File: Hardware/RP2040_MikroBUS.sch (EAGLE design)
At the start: 78 parts, among them J1 SWD, J3 Qwiic, J5 USB C, J6 microSD, J9 MIKROBUS_SMD_BLACK1, Q1 20V/4.2A/52mΩ/1.4W, U2 MAX17048, U3 MCP73831, U4 W25QXX128MBIT, U5 RP2040, U7 3.3V, Y2 12MHz

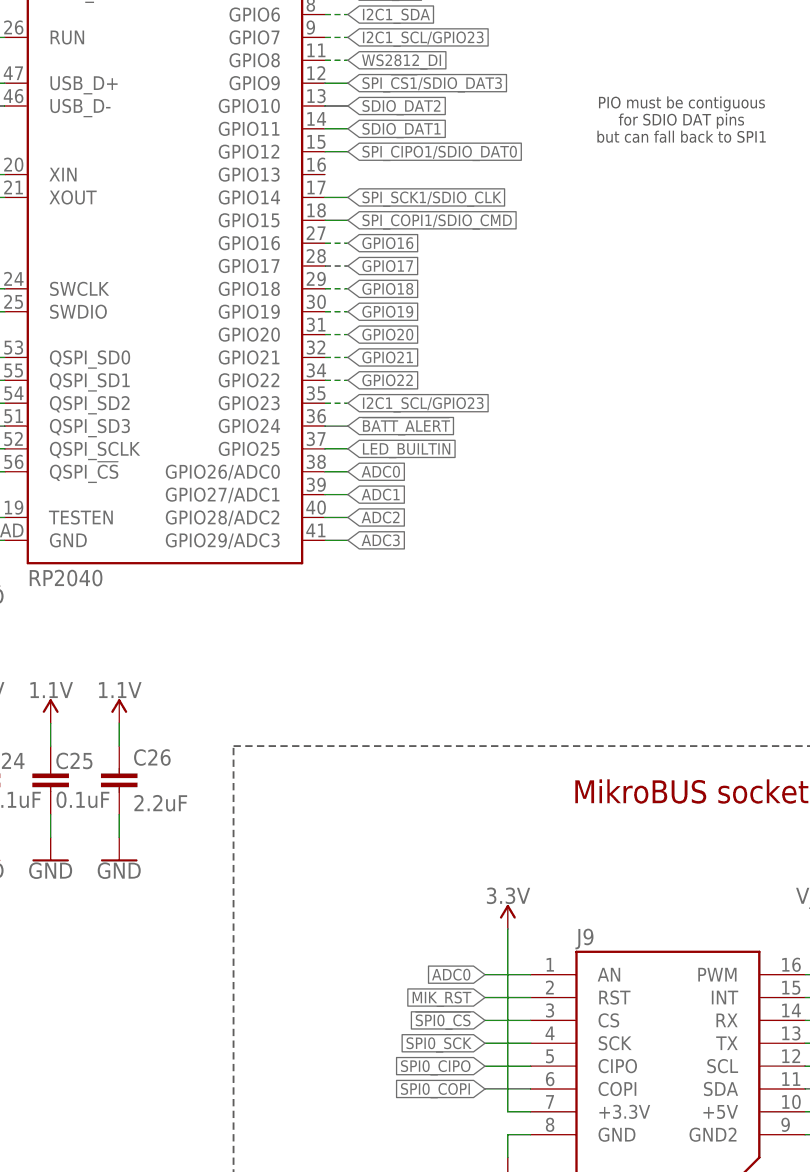
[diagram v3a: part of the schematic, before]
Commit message: From mikroE convo
* Remove reset button
* Remove CS pullup
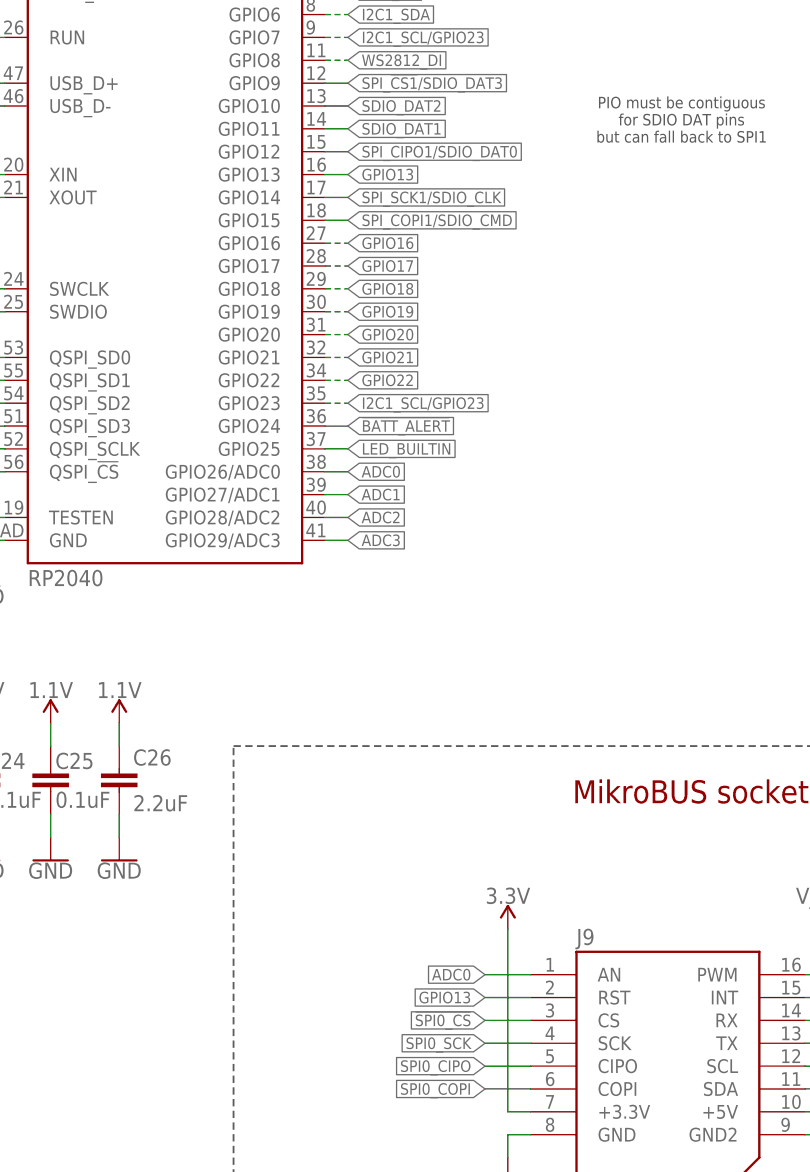
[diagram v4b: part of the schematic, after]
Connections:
- removed net MIK_RST: J9.RST
- new net GPIO13: J9.RST, U5.GPIO13
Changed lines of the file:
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@@
-</segment>
-</net>
-<net name="MIK_RST" class="0">
-<segment>
-<pinref part="J9" gate="J1" pin="RST"/>
-<wire x1="137.16" y1="38.1" x2="132.08" y2="38.1" width="0.1524" layer="91"/>
-<label x="132.08" y="38.1" size="1.27" layer="95" rot="R180" xref="yes"/>
 </segment>
 </net>
@@
 </segment>
 </net>
+<net name="GPIO13" class="0">
+<segment>
+<pinref part="U5" gate="U1" pin="GPIO13"/>
+<wire x1="114.3" y1="129.54" x2="116.84" y2="129.54" width="0.1524" layer="91"/>
+<label x="116.84" y="129.54" size="1.27" layer="95" xref="yes"/>
+</segment>
+<segment>
+<pinref part="J9" gate="J1" pin="RST"/>
+<wire x1="137.16" y1="38.1" x2="132.08" y2="38.1" width="0.1524" layer="91"/>
+<label x="132.08" y="38.1" size="1.27" layer="95" rot="R180" xref="yes"/>
+</segment>
+</net>

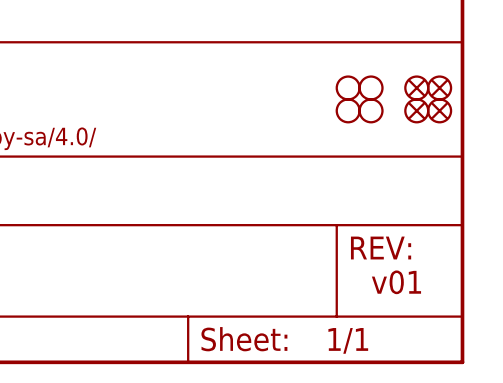
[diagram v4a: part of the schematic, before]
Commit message: Design review updates
* Bump version number
* Remove CS_PU label from borrom
* Move SWDCK TP
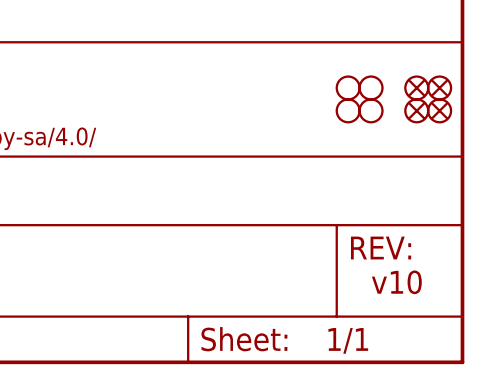
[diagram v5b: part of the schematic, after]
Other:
- note added: "v10"
- note removed: "v01"
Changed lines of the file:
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@@
 <text x="213.36" y="60.96" size="2.54" layer="94" font="vector" align="center">Status LED</text>
 <text x="381" y="101.6" size="2.54" layer="94" font="vector" align="center">Headers</text>
-<text x="421.64" y="10.16" size="2.54" layer="94" font="vector" align="top-left">v01</text>
+<text x="421.64" y="10.16" size="2.54" layer="94" font="vector" align="top-left">v10</text>
 <text x="292.1" y="187.96" size="2.54" layer="94" font="vector" align="center">Qwiic Connector</text>
 <text x="383.54" y="274.32" size="2.54" layer="94" font="vector" align="center">USB Connector</text>

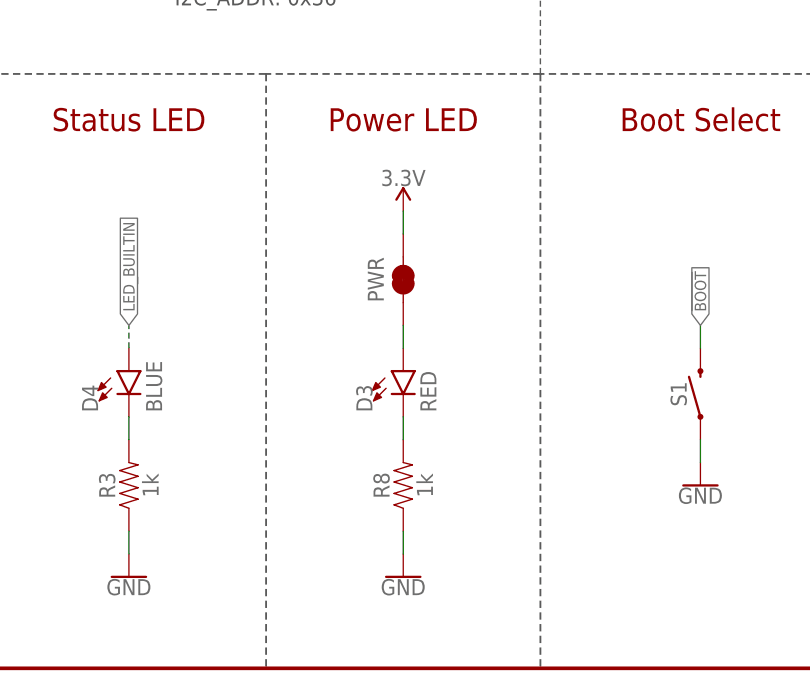
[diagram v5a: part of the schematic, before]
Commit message: QC Double check
* Added label for PWR jumper
* Moved GPIO16 via
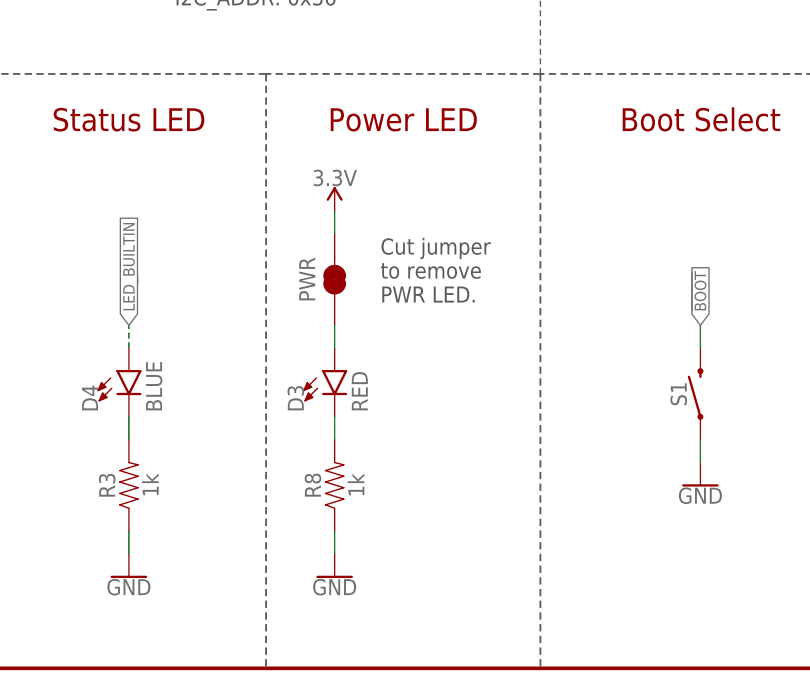
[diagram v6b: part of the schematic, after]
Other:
- note added: "Cut jumper to remove PWR LED."
- moved on the sheet: D3, PWR, R8
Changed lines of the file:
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@@
 <text x="354.076" y="11.43" size="2.54" layer="94" font="vector">Nick Poole</text>
 <text x="331.47" y="7.366" size="2.54" layer="94" font="vector">Revised by: Priyanka Makin</text>
+<text x="241.3" y="40.64" size="1.778" layer="97" font="vector">Cut jumper
+to remove
+PWR LED.</text>
 </plain>
 <instances>
@@
 <attribute name="VALUE" x="199.644" y="233.68" size="1.778" layer="96" font="vector" rot="R90" align="top-center"/>
 </instance>
-<instance part="R8" gate="G$1" x="243.84" y="20.32" smashed="yes" rot="R90">
-<attribute name="NAME" x="242.316" y="20.32" size="1.778" layer="95" font="vector" rot="R90" align="bottom-center"/>
-<attribute name="VALUE" x="245.364" y="20.32" size="1.778" layer="96" font="vector" rot="R90" align="top-center"/>
-</instance>
-<instance part="D3" gate="G$1" x="243.84" y="33.02" smashed="yes">
-<attribute name="NAME" x="240.411" y="28.448" size="1.778" layer="95" font="vector" rot="R90"/>
-<attribute name="VALUE" x="245.745" y="28.448" size="1.778" layer="96" font="vector" rot="R90" align="top-left"/>
-</instance>
-<instance part="GND41" gate="1" x="243.84" y="10.16" smashed="yes">
-<attribute name="VALUE" x="243.84" y="9.906" size="1.778" layer="96" align="top-center"/>
-</instance>
-<instance part="SUPPLY36" gate="G$1" x="243.84" y="50.8" smashed="yes">
-<attribute name="VALUE" x="243.84" y="53.594" size="1.778" layer="96" align="bottom-center"/>
+<instance part="R8" gate="G$1" x="236.22" y="20.32" smashed="yes" rot="R90">
+<attribute name="NAME" x="234.696" y="20.32" size="1.778" layer="95" font="vector" rot="R90" align="bottom-center"/>
+<attribute name="VALUE" x="237.744" y="20.32" size="1.778" layer="96" font="vector" rot="R90" align="top-center"/>
+</instance>
+<instance part="D3" gate="G$1" x="236.22" y="33.02" smashed="yes">
+<attribute name="NAME" x="232.791" y="28.448" size="1.778" layer="95" font="vector" rot="R90"/>
+<attribute name="VALUE" x="238.125" y="28.448" size="1.778" layer="96" font="vector" rot="R90" align="top-left"/>
+</instance>
+<instance part="GND41" gate="1" x="236.22" y="10.16" smashed="yes">
+<attribute name="VALUE" x="236.22" y="9.906" size="1.778" layer="96" align="top-center"/>
+</instance>
+<instance part="SUPPLY36" gate="G$1" x="236.22" y="50.8" smashed="yes">
+<attribute name="VALUE" x="236.22" y="53.594" size="1.778" layer="96" align="bottom-center"/>
 </instance>
 <instance part="GND42" gate="1" x="386.08" y="215.9" smashed="yes">
@@
 <attribute name="VALUE" x="226.06" y="154.686" size="1.778" layer="96" align="top-center"/>
 </instance>
-<instance part="PWR" gate="G$1" x="243.84" y="43.18" smashed="yes" rot="R90">
-<attribute name="NAME" x="240.792" y="43.18" size="1.778" layer="95" font="vector" rot="R90" align="center"/>
+<instance part="PWR" gate="G$1" x="236.22" y="43.18" smashed="yes" rot="R90">
+<attribute name="NAME" x="233.172" y="43.18" size="1.778" layer="95" font="vector" rot="R90" align="center"/>
 </instance>
 </instances>
@@
 <pinref part="PWR" gate="G$1" pin="2"/>
 <pinref part="SUPPLY36" gate="G$1" pin="3.3V"/>
-<wire x1="243.84" y1="48.26" x2="243.84" y2="50.8" width="0.1524" layer="91"/>
+<wire x1="236.22" y1="48.26" x2="236.22" y2="50.8" width="0.1524" layer="91"/>
 </segment>
 </net>
@@
 <segment>
 <pinref part="R8" gate="G$1" pin="1"/>
-<wire x1="243.84" y1="15.24" x2="243.84" y2="12.7" width="0.1524" layer="91"/>
+<wire x1="236.22" y1="15.24" x2="236.22" y2="12.7" width="0.1524" layer="91"/>
 <pinref part="GND41" gate="1" pin="GND"/>
 </segment>
@@
 <pinref part="D3" gate="G$1" pin="C"/>
 <pinref part="R8" gate="G$1" pin="2"/>
-<wire x1="243.84" y1="27.94" x2="243.84" y2="25.4" width="0.1524" layer="91"/>
+<wire x1="236.22" y1="27.94" x2="236.22" y2="25.4" width="0.1524" layer="91"/>
 </segment>
 </net>
@@
 <pinref part="D3" gate="G$1" pin="A"/>
 <pinref part="PWR" gate="G$1" pin="1"/>
-<wire x1="243.84" y1="35.56" x2="243.84" y2="38.1" width="0.1524" layer="91"/>
-</segment>
-</net>
+<wire x1="236.22" y1="35.56" x2="236.22" y2="38.1" width="0.1524" layer="91"/>
+</segment>
+</net>
